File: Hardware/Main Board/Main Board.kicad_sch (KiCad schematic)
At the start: 70 parts, among them J1 Micro_SD_Card_Det1, J3 Conn_01x09_Socket, J4 MIC 1 Connector, J5 MIC 2 Connector, J6 USB_C_Receptacle_USB2.0_16P, J7 OLED, J8 Conn_02x12_Counter_Clockwise, Q1 AO3401A, SW1 SW_SPST, U1 ESP32-S3-WROOM-2, U2 TPS63060, U3 TP4056-42-ESOP8

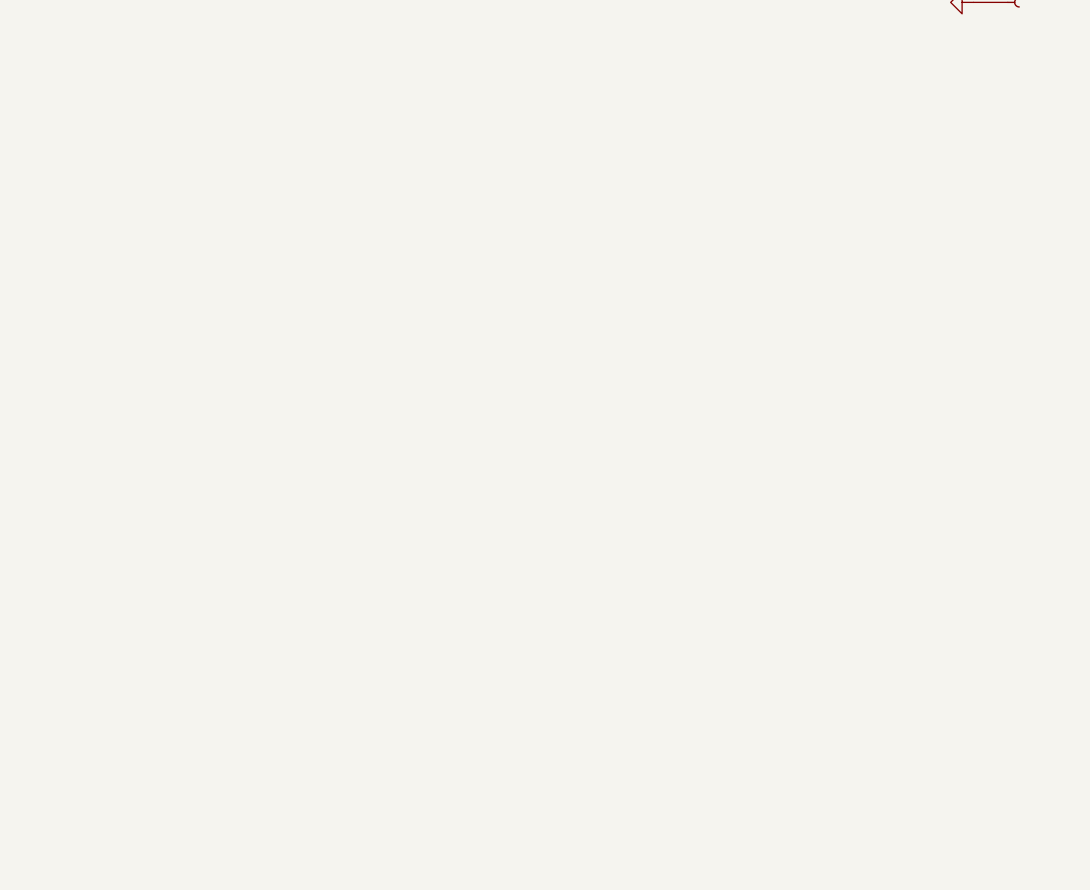
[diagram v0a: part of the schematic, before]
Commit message: ov2640 footprints
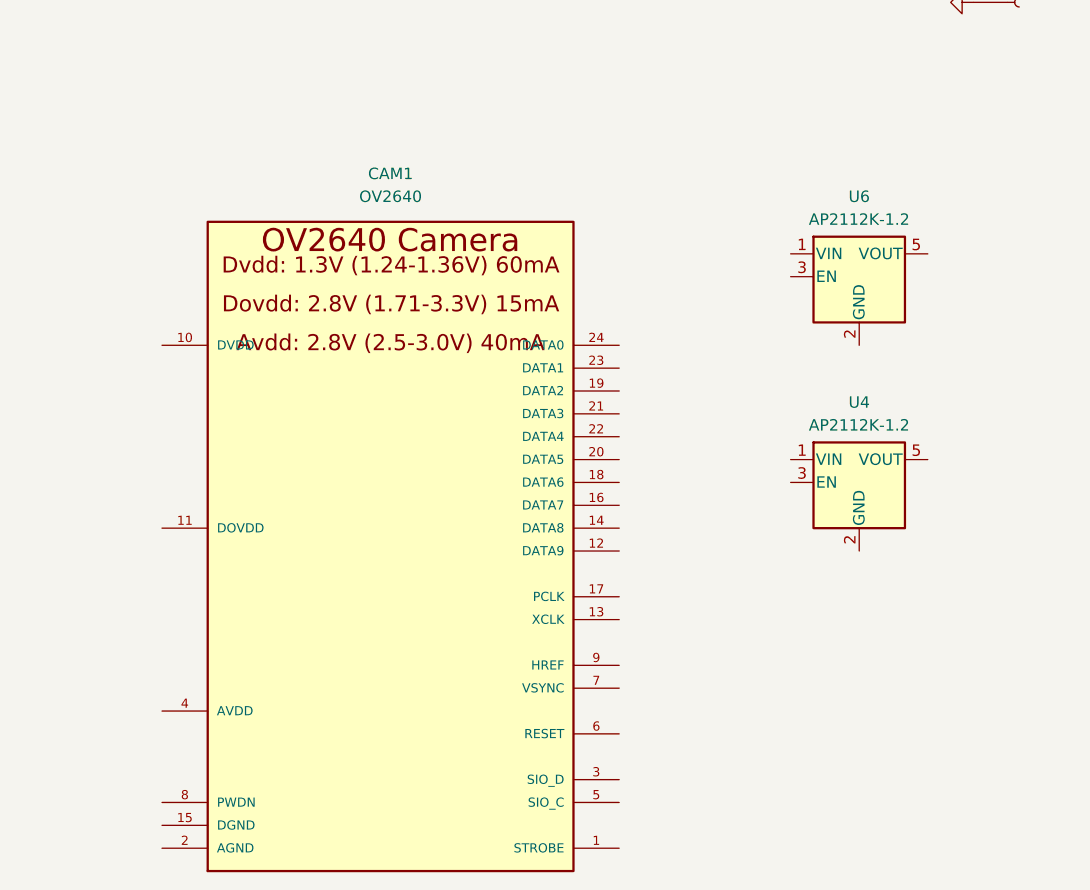
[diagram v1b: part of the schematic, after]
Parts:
- added CAM1: OV2640, OV2640:OV2640, symbol OV2640:OV2640
- added U4, U6: AP2112K-1.2, Package_TO_SOT_SMD:SOT-23-5, symbol Regulator_Linear:AP2112K-1.2
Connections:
- new net: CAM1.15 (DGND), CAM1.MT1 (DGND), CAM1.MT2 (DGND)

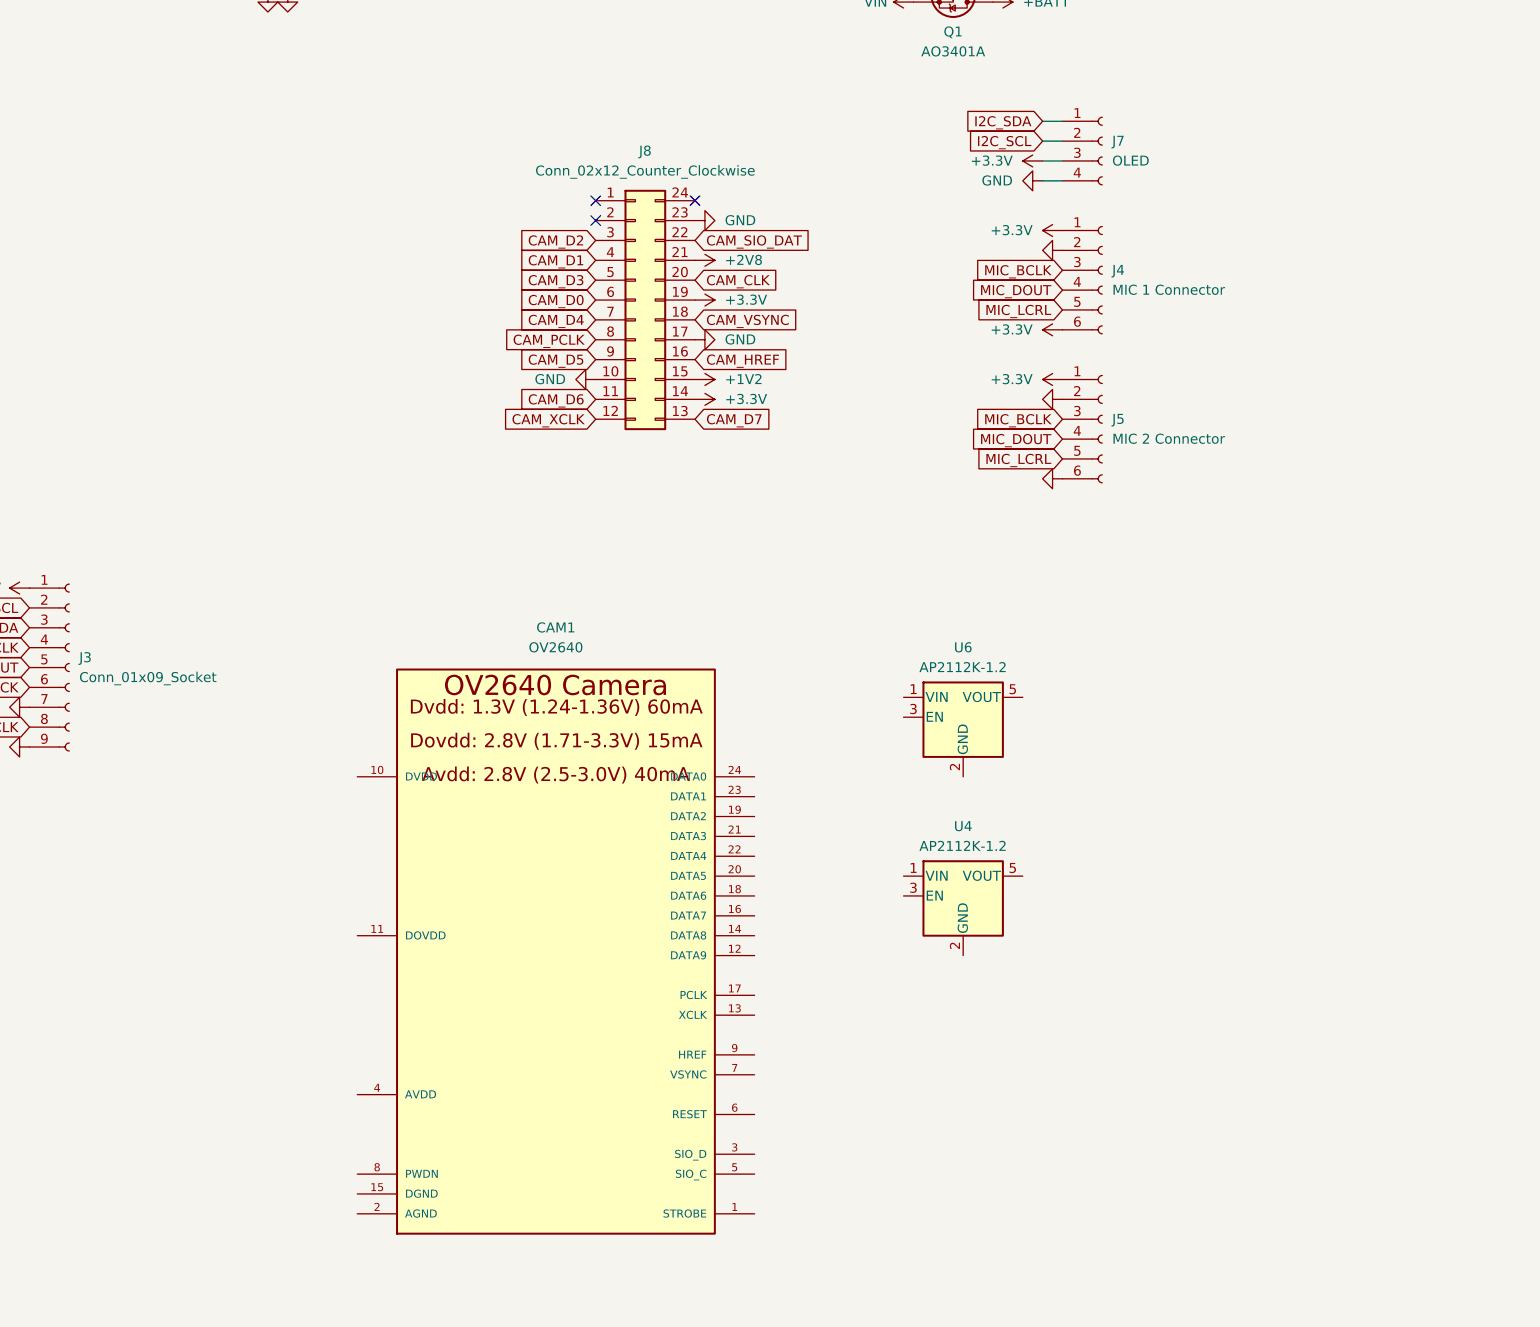
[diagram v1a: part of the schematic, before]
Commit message: finished ov2640 schematic
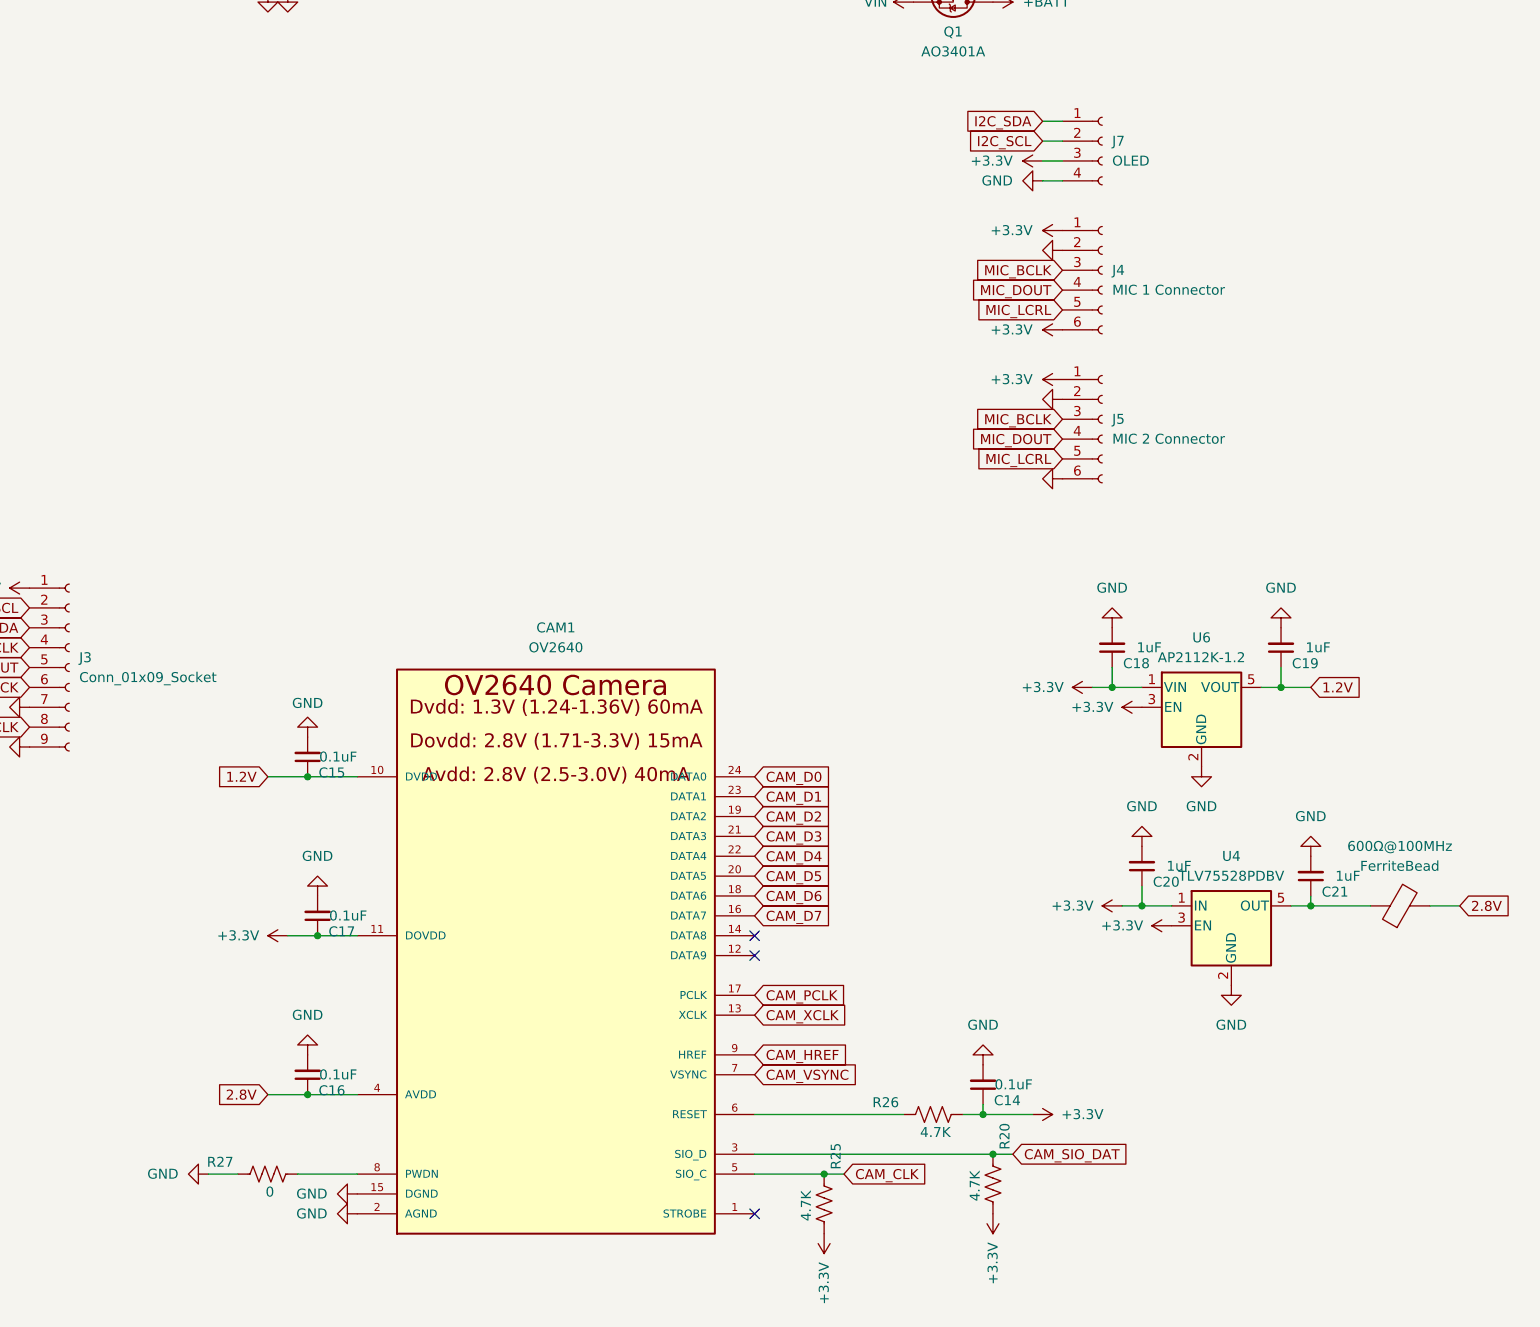
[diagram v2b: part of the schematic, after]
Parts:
- removed J8: Conn_02x12_Counter_Clockwise, Connector_FFC-FPC:Hirose_FH12-24S-0.5SH_1x24-1MP_P0.50mm_Horizontal, symbol Connector_Generic:Conn_02x12_Counter_Clockwise
- removed U4: AP2112K-1.2, Package_TO_SOT_SMD:SOT-23-5, symbol Regulator_Linear:AP2112K-1.2
- added 600Ω@100MHz: FerriteBead, symbol Device:FerriteBead
- added C14, C15, C16, C17: 0.1uF, Capacitor_SMD:C_0603_1608Metric, symbol Device:C_Small
- added C18, C19, C20, C21: 1uF, Capacitor_SMD:C_0603_1608Metric, symbol Device:C_Small
- added R20, R25, R26: 4.7K, Resistor_SMD:R_0402_1005Metric, symbol Device:R_US
- added R27: 0, Resistor_SMD:R_0402_1005Metric, symbol Device:R_US
- added U4: TLV75528PDBV, Package_TO_SOT_SMD:SOT-23-5, symbol Regulator_Linear:TLV75528PDBV
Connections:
- net +3.3V: now also CAM1.11 (DOVDD), U6.1 (VIN), U6.3 (EN), C14.1, C17.1, C18.1, C20.1, R20.1, R25.1, R26.1, U4.1 (IN), U4.3 (EN)
- net CAM_CLK: now also CAM1.5 (SIO_C), R25.2
- net CAM_D0: now also CAM1.24 (DATA0)
- net CAM_D1: now also CAM1.23 (DATA1)
- net CAM_D2: now also CAM1.19 (DATA2)
- net CAM_D3: now also CAM1.21 (DATA3)
- net CAM_D4: now also CAM1.22 (DATA4)
- net CAM_D5: now also CAM1.20 (DATA5)
- net CAM_D6: now also CAM1.18 (DATA6)
- net CAM_D7: now also CAM1.16 (DATA7)
- net CAM_HREF: now also CAM1.9 (HREF)
- net CAM_PCLK: now also CAM1.17 (PCLK)
- net CAM_SIO_DAT: now also CAM1.3 (SIO_D), R20.2
- net CAM_VSYNC: now also CAM1.7 (VSYNC)
- net CAM_XCLK: now also CAM1.13 (XCLK)
- net GND: now also CAM1.15 (DGND), CAM1.2 (AGND), CAM1.MT1 (DGND), CAM1.MT2 (DGND), U6.2 (GND), C14.2, C15.2, C16.2, C17.2, C18.2, C19.2, C20.2, C21.2, R27.2, U4.2 (GND)
- net 1.2V: now reaches U6.5 (VOUT)
- net 1.2V: now also CAM1.10 (DVDD), C15.1, C19.1
- net 2.8V: now reaches CAM1.4 (AVDD)
- net 2.8V: now also 600Ω@100MHz.2, C16.1
- net at CAM1.6 (RESET): now also R26.2
- net at CAM1.8 (PWDN): now also R27.1
- new net: 600Ω@100MHz.1, C21.1, U4.5 (OUT)
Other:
- moved on the sheet: U6

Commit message: camera pcb
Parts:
- renumbered 600Ω@100MHz to 600Ω@100MHz1
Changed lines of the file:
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@@
 		(dnp no)
 		(fields_autoplaced yes)
-		(property "Reference" "600Ω@100MHz"
+		(property "Reference" "600Ω@100MHz1"
 			(at 319.9892 208.28 90)
 			(effects
@@
 			(project ""
 				(path "/06300a21-1646-41b0-b473-1c39557d6dab"
-					(reference "600Ω@100MHz")
+					(reference "600Ω@100MHz1")
 					(unit 1)
 				)

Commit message: finished camera pcb
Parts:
- removed R8: 22, Resistor_SMD:R_0402_1005Metric, symbol Device:R_US
- added R28: 22, Resistor_SMD:R_0402_1005Metric, symbol Device:R_US
- 600Ω@100MHz1: footprint (none) -> Resistor_SMD:R_0603_1608Metric
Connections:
- net CAM_D0: now also U1.15 (IO3); no longer U1.24 (IO47)
- net CAM_D1: now also U1.16 (IO46); no longer U1.25 (IO48)
- net CAM_D2: now also U1.20 (IO12); no longer U1.22 (IO14)
- net CAM_D3: now also U1.18 (IO10); no longer U1.23 (IO21)
- net CAM_D4: now also U1.17 (IO9); no longer U1.20 (IO12)
- net CAM_D5: now also U1.19 (IO11); no longer U1.21 (IO13)
- net CAM_D6: now also U1.21 (IO13); no longer U1.18 (IO10)
- net CAM_D7: now also U1.23 (IO21); no longer U1.19 (IO11)
- net CAM_PCLK: now also R28.2
- net CAM_VSYNC: now also U1.25 (IO48); no longer U1.15 (IO3)
- net at R23.1: now also U1.24 (IO47); no longer U1.17 (IO9)
- new net: R28.1, U1.22 (IO14)
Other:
- moved on the sheet: R23

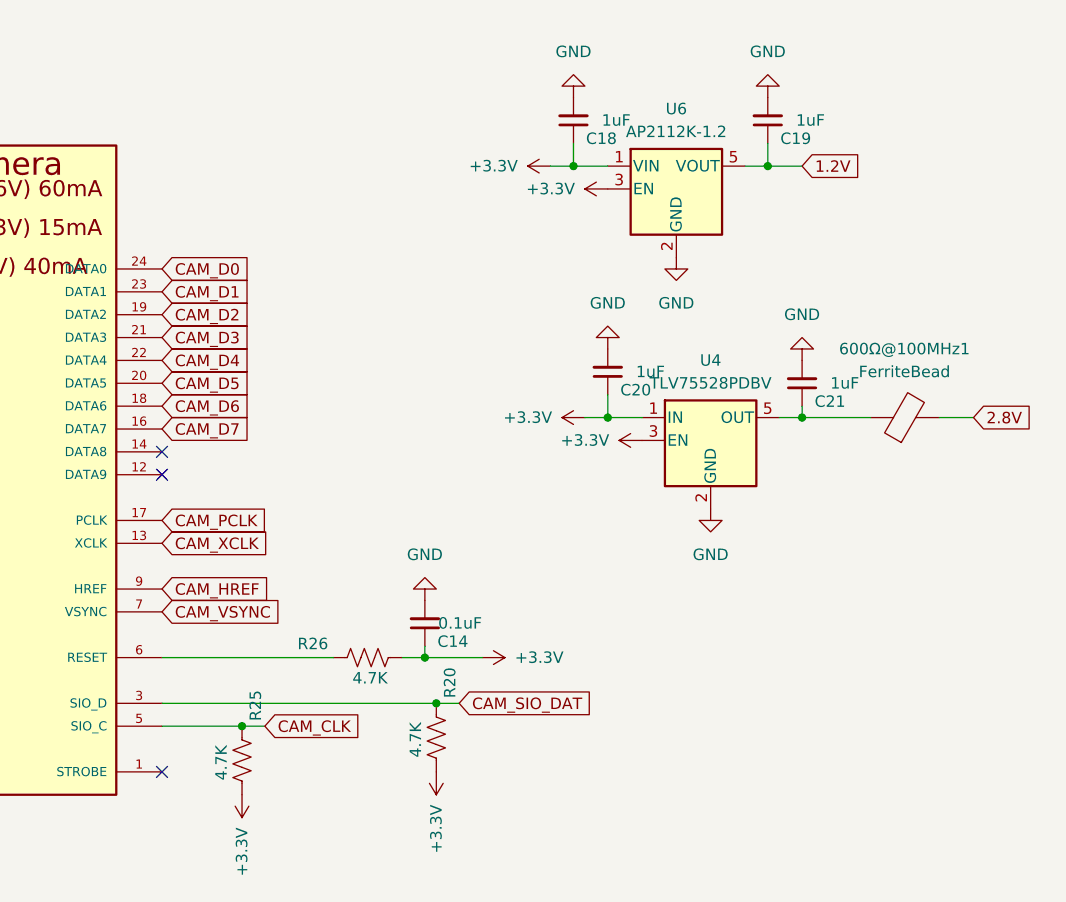
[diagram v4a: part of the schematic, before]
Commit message: reviewed kevin's layout, changed boot reset buttons and updated layout
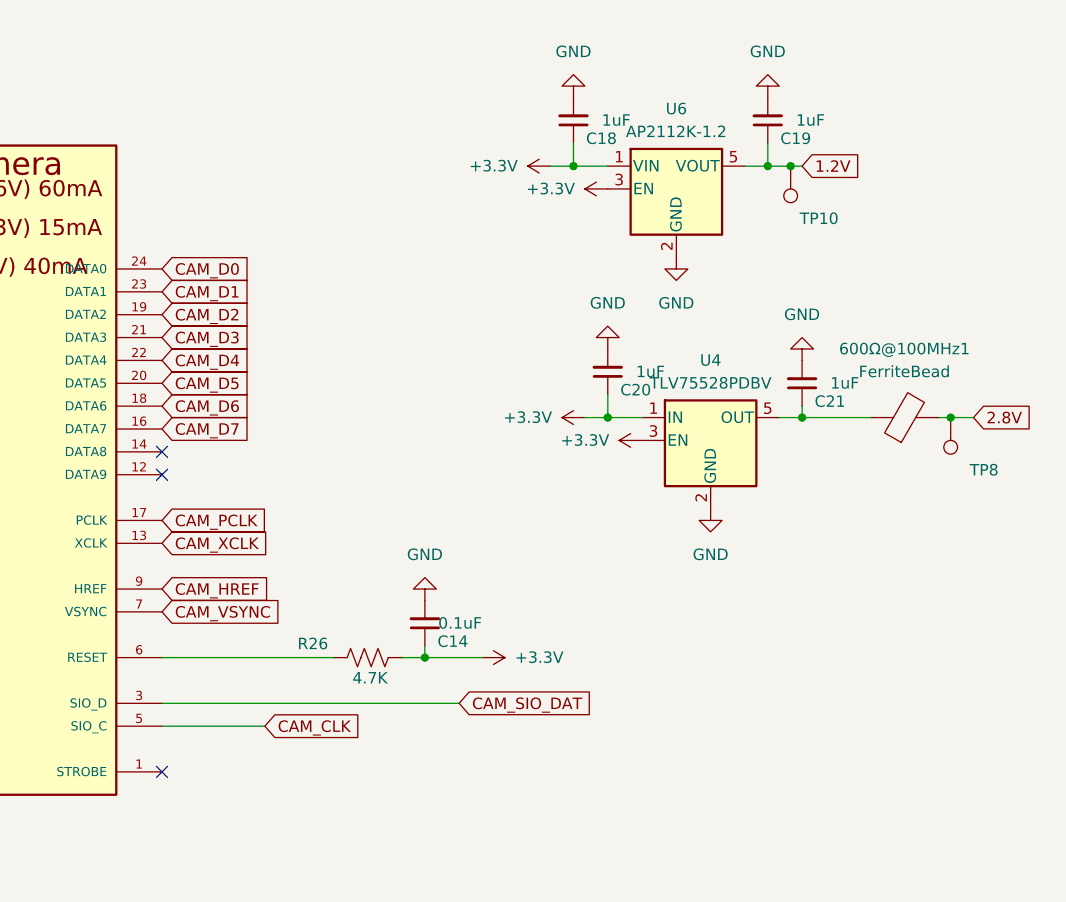
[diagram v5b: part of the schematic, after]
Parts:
- removed R20, R25: 4.7K, Resistor_SMD:R_0402_1005Metric, symbol Device:R_US
- added TP10, TP8: TestPoint, TestPoint:TestPoint_Pad_1.0x1.0mm, symbol Connector:TestPoint
- BOOT1, RESET1: footprint Button_Switch_SMD:SW_SPST_EVQP7A -> Button_Switch_SMD:SW_Tactile_SPST_NO_Straight_CK_PTS636Sx25SMTRLFS
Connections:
- net 1.2V: now also TP10.1
- net 2.8V: now also TP8.1
